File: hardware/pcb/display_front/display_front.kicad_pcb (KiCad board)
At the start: 2 copper layers, 62.2 x 21.6 mm, 6 parts, among them J10 GND_IN, J5 DISP_ANODES, J6 DISP_CATHODES, J9 VCC_IN

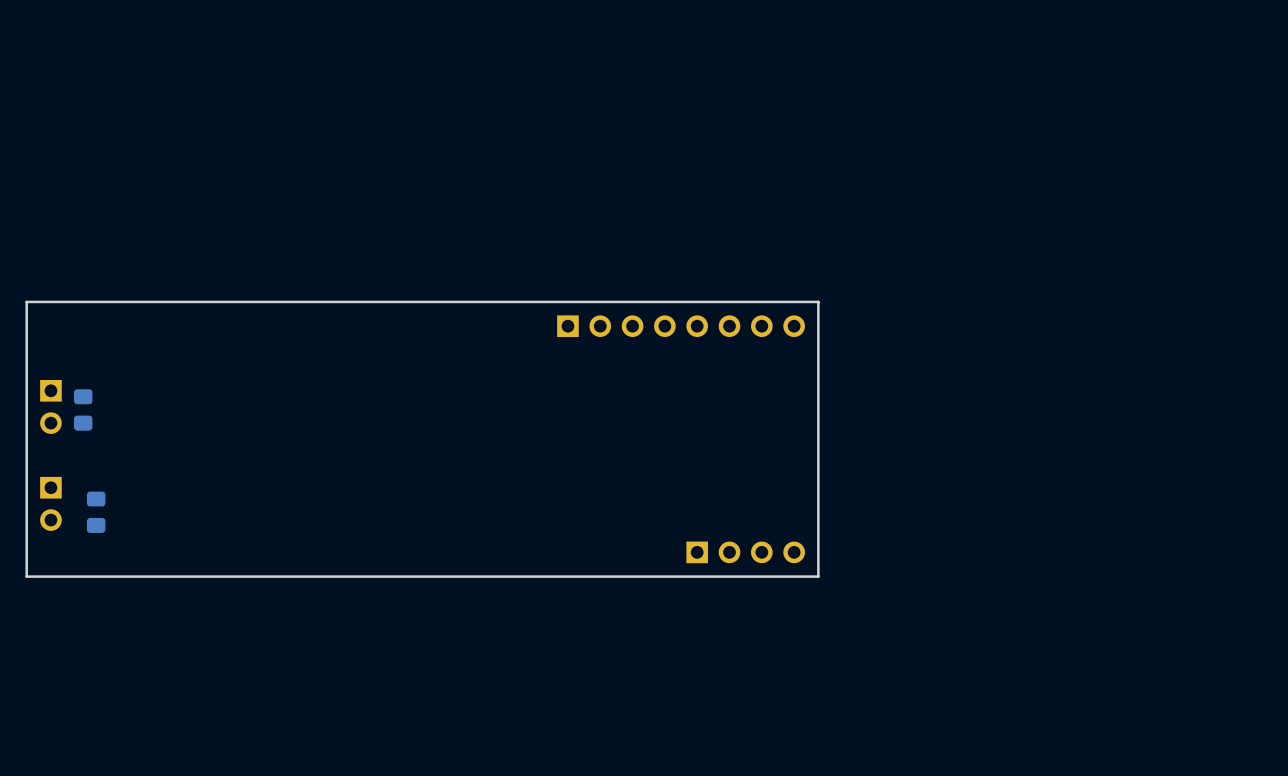
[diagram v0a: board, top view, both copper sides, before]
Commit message: Display front schematics
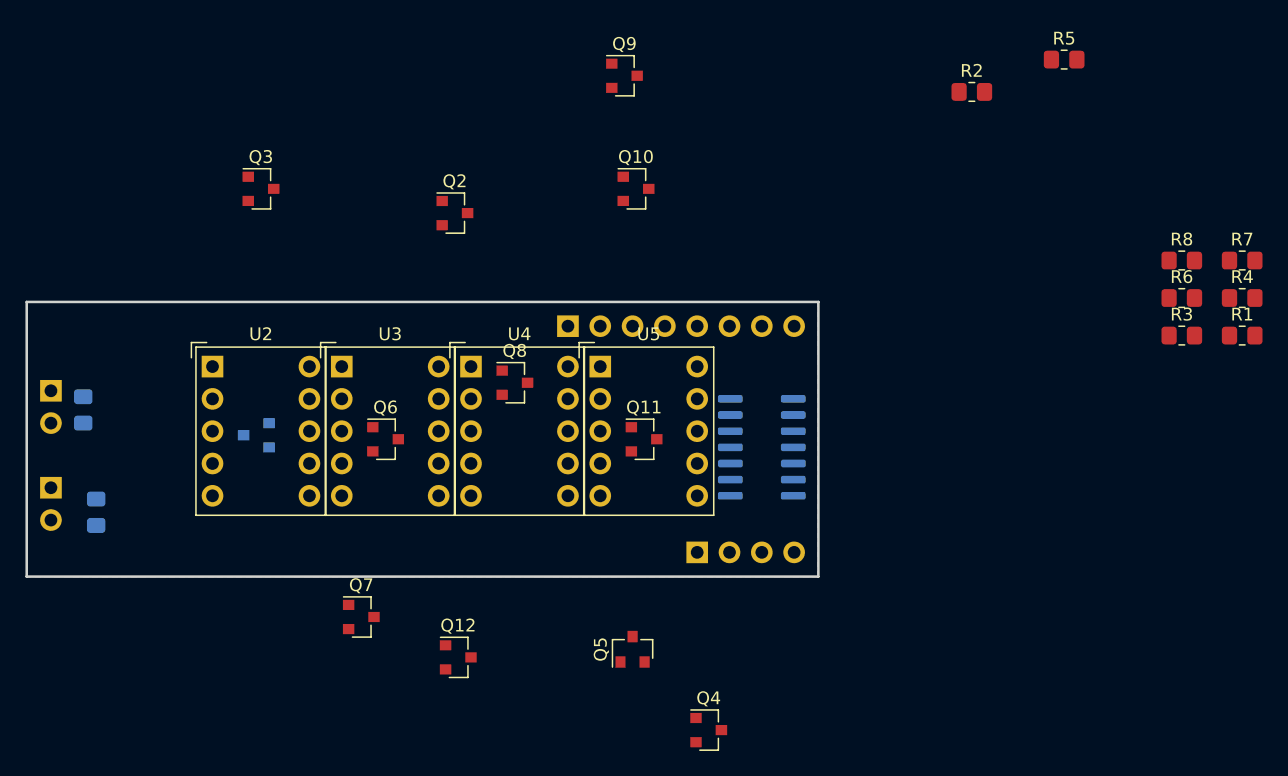
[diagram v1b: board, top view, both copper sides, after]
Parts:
- added Q1: Q_NMOS_GSD, Package_TO_SOT_SMD:SOT-23, B.Cu at (53.0, 46.7)
- added Q10: Q_NMOS_GSD, Package_TO_SOT_SMD:SOT-23, F.Cu at (82.8, 27.3)
- added Q11: Q_NMOS_GSD, Package_TO_SOT_SMD:SOT-23, F.Cu at (83.5, 47.0)
- added Q12: Q_NMOS_GSD, Package_TO_SOT_SMD:SOT-23, F.Cu at (68.8, 64.1)
- added Q2: Q_NMOS_GSD, Package_TO_SOT_SMD:SOT-23, F.Cu at (68.6, 29.2)
- added Q3: Q_NMOS_GSD, Package_TO_SOT_SMD:SOT-23, F.Cu at (53.3, 27.3)
- added Q4: Q_NMOS_GSD, Package_TO_SOT_SMD:SOT-23, F.Cu at (88.5, 69.8)
- added Q5: Q_NMOS_GSD, Package_TO_SOT_SMD:SOT-23, F.Cu at (82.5, 63.5)
- added Q6: Q_NMOS_GSD, Package_TO_SOT_SMD:SOT-23, F.Cu at (63.1, 47.0)
- added Q7: Q_NMOS_GSD, Package_TO_SOT_SMD:SOT-23, F.Cu at (61.2, 61.0)
- added Q8: Q_NMOS_GSD, Package_TO_SOT_SMD:SOT-23, F.Cu at (73.3, 42.5)
- added Q9: Q_NMOS_GSD, Package_TO_SOT_SMD:SOT-23, F.Cu at (81.9, 18.4)
- added R1: 100, Resistor_SMD:R_0805_2012Metric_Pad1.20x1.40mm_HandSolder, F.Cu at (130.5, 38.8)
- added R2: 100, Resistor_SMD:R_0805_2012Metric_Pad1.20x1.40mm_HandSolder, F.Cu at (109.2, 19.7)
- added R3: 100, Resistor_SMD:R_0805_2012Metric_Pad1.20x1.40mm_HandSolder, F.Cu at (125.7, 38.8)
- added R4: 100, Resistor_SMD:R_0805_2012Metric_Pad1.20x1.40mm_HandSolder, F.Cu at (130.5, 35.9)
- added R5: 100, Resistor_SMD:R_0805_2012Metric_Pad1.20x1.40mm_HandSolder, F.Cu at (116.5, 17.1)
- added R6: 100, Resistor_SMD:R_0805_2012Metric_Pad1.20x1.40mm_HandSolder, F.Cu at (125.7, 35.9)
- added R7: 100, Resistor_SMD:R_0805_2012Metric_Pad1.20x1.40mm_HandSolder, F.Cu at (130.5, 32.9)
- added R8: 100, Resistor_SMD:R_0805_2012Metric_Pad1.20x1.40mm_HandSolder, F.Cu at (125.7, 32.9)
- added U1: 74HC04, Package_SO:SOIC-14_3.9x8.7mm_P1.27mm, B.Cu at (92.7, 47.6)
- added U2: SC39-11GWA, Display_7Segment:Sx39-1xxxxx, F.Cu at (49.5, 41.3)
- added U3: SC39-11GWA, Display_7Segment:Sx39-1xxxxx, F.Cu at (59.7, 41.3)
- added U4: SC39-11GWA, Display_7Segment:Sx39-1xxxxx, F.Cu at (69.8, 41.3)
- added U5: SC39-11GWA, Display_7Segment:Sx39-1xxxxx, F.Cu at (80.0, 41.3)
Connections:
- J5 pad 1: (no net) -> DA
- J5 pad 2: (no net) -> DB
- J5 pad 3: (no net) -> DC
- J5 pad 4: (no net) -> DD
- J5 pad 5: (no net) -> DE
- J5 pad 6: (no net) -> DF
- J5 pad 7: (no net) -> DG
- J5 pad 8: (no net) -> DDP
- J6 pad 1: (no net) -> CA0
- J6 pad 2: (no net) -> CA1
- J6 pad 3: (no net) -> CA2
- J6 pad 4: (no net) -> CA3

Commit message: Routed
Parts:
- Q10, Q11, Q12, Q2, Q3, Q4, Q5, Q6, Q7, Q8, Q9, R1, R2, R3, R4, R5, R6, R7, R8: moved to B.Cu
- moved R4 83.8 mm to (48.9, 55.0), turned to 180 degrees
- moved R1 81.5 mm to (49.0, 39.8), turned to 180 degrees
- moved R3 67.9 mm to (59.8, 55.0), turned to 180 degrees
- moved R5 59.6 mm to (70.5, 55.0), turned to 180 degrees
- moved R7 57.6 mm to (73.3, 39.6)
- moved R6 57.3 mm to (68.6, 39.6), turned to 180 degrees
- moved R2 53.3 mm to (59.8, 39.8), turned to 180 degrees
- moved C9 51.0 mm to (90.3, 41.9), turned to 0 degrees
- moved R8 49.6 mm to (81.3, 55.0), turned to 180 degrees
- moved Q4 34.0 mm to (59.7, 51.8), turned to 180 degrees
- moved Q5 30.8 mm to (59.7, 42.9), turned to 180 degrees
- moved Q9 27.1 mm to (70.5, 42.9), turned to 180 degrees
- moved Q3 24.9 mm to (48.9, 51.8), turned to 180 degrees
- moved Q2 24.0 mm to (48.9, 42.9), turned to 180 degrees
- moved Q12 17.5 mm to (81.3, 51.8), turned to 180 degrees
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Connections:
- Q3 pad 1: DB -> DD
- Q3 pad 2: B -> D
- Q5 pad 1: DD -> DB
- Q5 pad 2: D -> B
- R2 pad 2: Net-(Q3-Pad3) -> Net-(Q5-Pad3)
- R4 pad 2: Net-(Q5-Pad3) -> Net-(Q3-Pad3)
- U1 pad 1: CA3 -> GND
- U1 pad 10: (no net) -> Net-(Q8-Pad1)
- U1 pad 11: GND -> CA1
- U1 pad 12: (no net) -> Net-(Q11-Pad1)
- U1 pad 13: GND -> CA0
- U1 pad 2: Net-(Q1-Pad1) -> (no net)
- U1 pad 3: CA2 -> GND
- U1 pad 4: Net-(Q6-Pad1) -> (no net)
- U1 pad 5: CA1 -> CA3
- U1 pad 6: Net-(Q8-Pad1) -> Net-(Q1-Pad1)
- U1 pad 8: Net-(Q11-Pad1) -> Net-(Q6-Pad1)
- U1 pad 9: CA0 -> CA2
- U2 pad 3: (no net) -> Net-(Q1-Pad3)
- U3 pad 3: (no net) -> Net-(Q6-Pad3)
- U4 pad 3: (no net) -> Net-(Q8-Pad3)
- U5 pad 3: (no net) -> Net-(Q11-Pad3)
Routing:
- net Net-(Q1-Pad1): track 0.00 -> 64.1 mm, vias 0 -> 2
- net Net-(Q6-Pad1): track 0.00 -> 48.9 mm, vias 0 -> 2
- net DD: track 0.00 -> 45.3 mm, vias 0 -> 1
- net D: track 0.00 -> 41.6 mm
- net E: track 0.00 -> 41.5 mm
- net G: track 0.00 -> 40.8 mm
- net F: track 0.00 -> 40.5 mm
- net Net-(Q8-Pad1): track 0.00 -> 40.1 mm, vias 0 -> 2
- net C: track 0.00 -> 40.0 mm
- net A: track 0.00 -> 38.8 mm
- net B: track 0.00 -> 38.5 mm
- net DP: track 0.00 -> 38.2 mm
- net DC: track 0.00 -> 31.8 mm, vias 0 -> 1
- net DA: track 0.00 -> 29.2 mm, vias 0 -> 1
- net DE: track 0.00 -> 25.4 mm, vias 0 -> 1
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
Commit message: Add silk for front
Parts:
- J10: value GND_IN -> GND
- J5: value DISP_ANODES -> Anodes
- J6: value DISP_CATHODES -> Cathodes
- J9: value VCC_IN -> VCC
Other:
- board text added: "JLCJLCJLCJLC"
- board text added: "Output (front) v1.0"
- board text added: "Velko 2021"

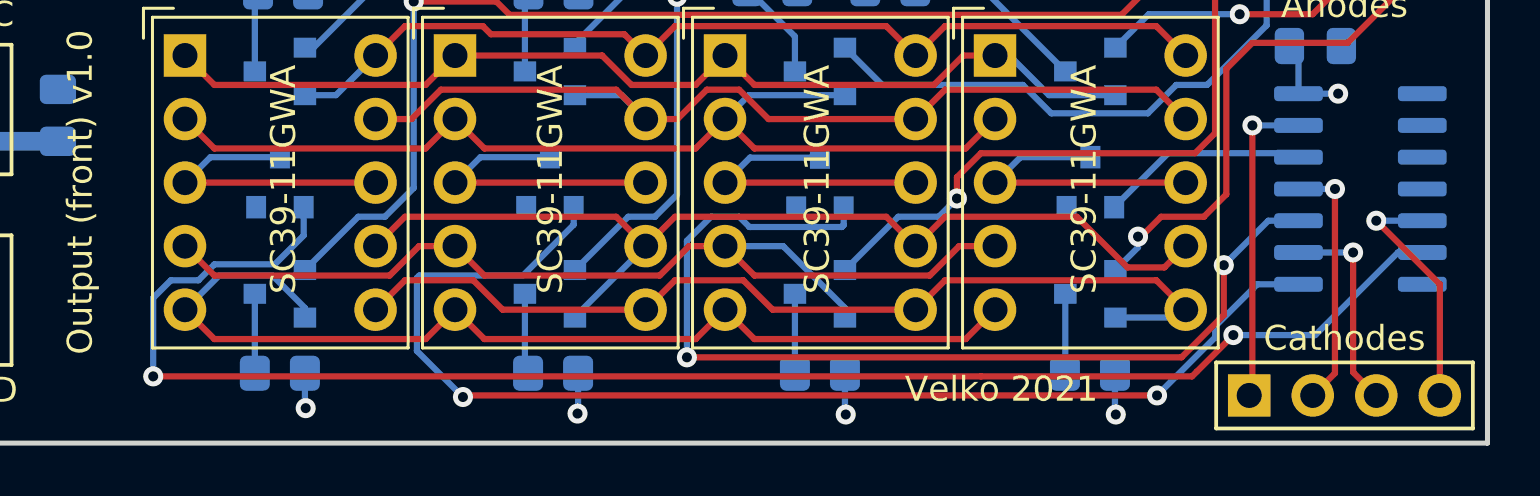
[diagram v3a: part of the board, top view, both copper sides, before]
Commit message: Improve ground plane
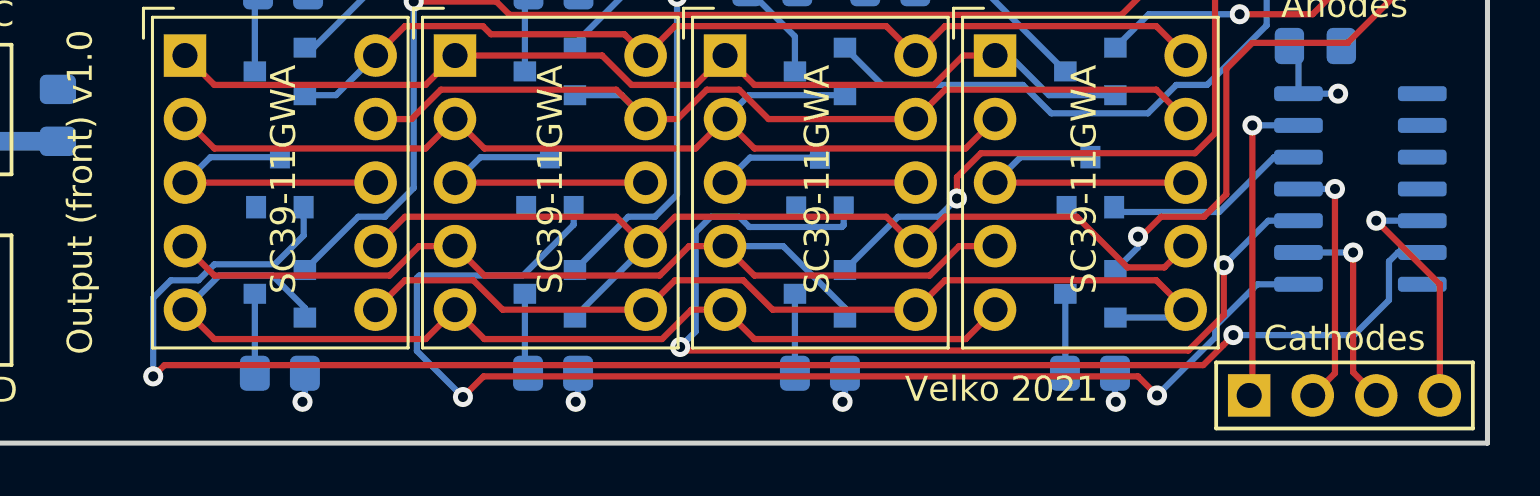
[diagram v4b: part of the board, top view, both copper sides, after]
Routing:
- net VCC: track 21.5 -> 19.9 mm
- net Net-(Q1-Pad1): track 64.1 -> 65.0 mm
- net Net-(Q6-Pad1): track 48.9 -> 49.5 mm
